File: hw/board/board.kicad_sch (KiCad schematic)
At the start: 21 parts, among them J1 DE9_Receptacle, J2 DE9_Receptacle, J3 DE9_Receptacle, J4 DE9_Receptacle, J5 DE9_Receptacle, J6 DE9_Receptacle, J7 DE9_Receptacle, J8 DE9_Receptacle, U1 XC7A35T-FTG256

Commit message: Added decoupling network following Xiling UG483
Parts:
- added C1, C14, C17, C18, C19, C2, C24, C25, C26, C27, C28, C29, C34, C35, C36, C37, C38, C39, C40: 470n, Capacitor_SMD:C_0805_2012Metric_Pad1.18x1.45mm_HandSolder, symbol Device:C
- added C13, C15: 47u, Capacitor_SMD:C_0805_2012Metric_Pad1.18x1.45mm_HandSolder, symbol Device:C
- added C16: 100u, Capacitor_SMD:C_0805_2012Metric_Pad1.18x1.45mm_HandSolder, symbol Device:C
- added C22, C23, C30, C31, C32, C33: 4u7, Capacitor_SMD:C_0805_2012Metric_Pad1.18x1.45mm_HandSolder, symbol Device:C
- C10, C11, C3: value 4u7 -> 470n; footprint Capacitor_SMD:C_0805_2012Metric -> Capacitor_SMD:C_0805_2012Metric_Pad1.18x1.45mm_HandSolder
- C12: value 100u -> 470n; footprint Capacitor_SMD:C_0805_2012Metric -> Capacitor_SMD:C_0805_2012Metric_Pad1.18x1.45mm_HandSolder
- C20: renamed from C2; footprint Capacitor_SMD:C_0805_2012Metric -> Capacitor_SMD:C_0805_2012Metric_Pad1.18x1.45mm_HandSolder
- C21: renamed from C1; value 100u -> 4u7; footprint Capacitor_SMD:C_0805_2012Metric -> Capacitor_SMD:C_0805_2012Metric_Pad1.18x1.45mm_HandSolder
- C4: value 100u -> 4u7; footprint Capacitor_SMD:C_0805_2012Metric -> Capacitor_SMD:C_0805_2012Metric_Pad1.18x1.45mm_HandSolder
- C5, C7, C8, C9: footprint Capacitor_SMD:C_0805_2012Metric -> Capacitor_SMD:C_0805_2012Metric_Pad1.18x1.45mm_HandSolder
- C6: value 4u7 -> 47u; footprint Capacitor_SMD:C_0805_2012Metric -> Capacitor_SMD:C_0805_2012Metric_Pad1.18x1.45mm_HandSolder
- renumbered J3 to J2, J5 to J3, J7 to J4, J2 to J5, J4 to J6, J6 to J7
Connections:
- net +1V0: now also C10.1, C11.1, C12.1, C7.1, C8.1, C9.1, U1.F7 (VCCINT), U1.F9 (VCCINT), U1.G6 (VCCINT), U1.H9 (VCCINT), U1.J6 (VCCINT), U1.K9 (VCCINT), U1.L8 (VCCINT), C13.1, C14.1
- net +3V3: now also C15.1, C16.1, C17.1, C18.1, C19.1, C22.1, C23.1, C24.1, C25.1, C26.1, C27.1, C28.1, C29.1, C30.1, C31.1, C32.1, C33.1, C34.1, C35.1, C36.1, C37.1, C38.1, C39.1, C40.1; no longer C10.1, C11.1, C12.1, C3.1, C4.1, C5.1, C6.1, C7.1, C8.1, C9.1
- net GND: now also U1.A1 (GND), U1.A11 (GND), U1.B8 (GND), U1.C15 (GND), U1.C5 (GND), U1.D12 (GND), U1.D2 (GND), U1.E9 (GND), U1.F10 (GND), U1.F16 (GND), U1.F6 (GND), U1.F8 (VCCBATT_0), U1.G13 (GND), U1.G3 (GND), U1.G7 (GNDADC_0), U1.G8 (VCCADC_0), U1.G9 (GND), U1.H6 (GND), U1.J11 (GND), U1.J9 (GND), U1.K14 (GND), U1.K4 (GND), U1.K6 (GND), U1.L1 (GND), U1.L11 (GND), U1.M8 (GND), U1.N15 (GND), U1.N5 (GND), U1.P12 (GND), U1.P2 (GND), U1.R9 (GND), U1.T16 (GND), U1.T6 (GND), C1.2, C13.2, C14.2, C15.2, C16.2, C17.2, C18.2, C19.2, C2.2, C22.2, C23.2, C24.2, C25.2, C26.2, C27.2, C28.2, C29.2, C30.2, C31.2, C32.2, C33.2, C34.2, C35.2, C36.2, C37.2, C38.2, C39.2, C40.2
- net +1V8: now reaches U1.G10 (VCCAUX)
- net +1V8: now also C3.1, C4.1, C5.1, C6.1, U1.J10 (VCCAUX), U1.K11 (VCCAUX), U1.L10 (VCCAUX), C1.1, C2.1
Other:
- moved on the sheet: C20, C21, U1A, U1B, U1C, U1D

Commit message: Added DE9 connector footprint
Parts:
- removed C1, C10, C11, C12, C14, C17, C18, C19, C2, C24, C25, C26, C27, C28, C29, C3, C34, C35, C36, C37, C38, C39, C40: 470n, Capacitor_SMD:C_0805_2012Metric_Pad1.18x1.45mm_HandSolder, symbol Device:C
- removed C13, C6: 47u, Capacitor_SMD:C_0805_2012Metric_Pad1.18x1.45mm_HandSolder, symbol Device:C
- removed C16, C7: 100u, Capacitor_SMD:C_0805_2012Metric_Pad1.18x1.45mm_HandSolder, symbol Device:C
- removed C20, C21, C22, C23, C30, C31, C32, C33, C4, C5, C8, C9: 4u7, Capacitor_SMD:C_0805_2012Metric_Pad1.18x1.45mm_HandSolder, symbol Device:C
- removed J1, J2, J3, J4, J5, J6, J7, J8: DE9_Receptacle, DE9:DE9_Pins, symbol Connector:DE9_Receptacle
- removed unit 4 of U1
- renumbered C15 to C1
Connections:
- net +3V3 renamed +2V5
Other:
- added sheet PDN (PDN.kicad_sch)
- added sheet SpW Connection (SpW.kicad_sch)
- moved on the sheet: C1, U1A, U1B, U1C

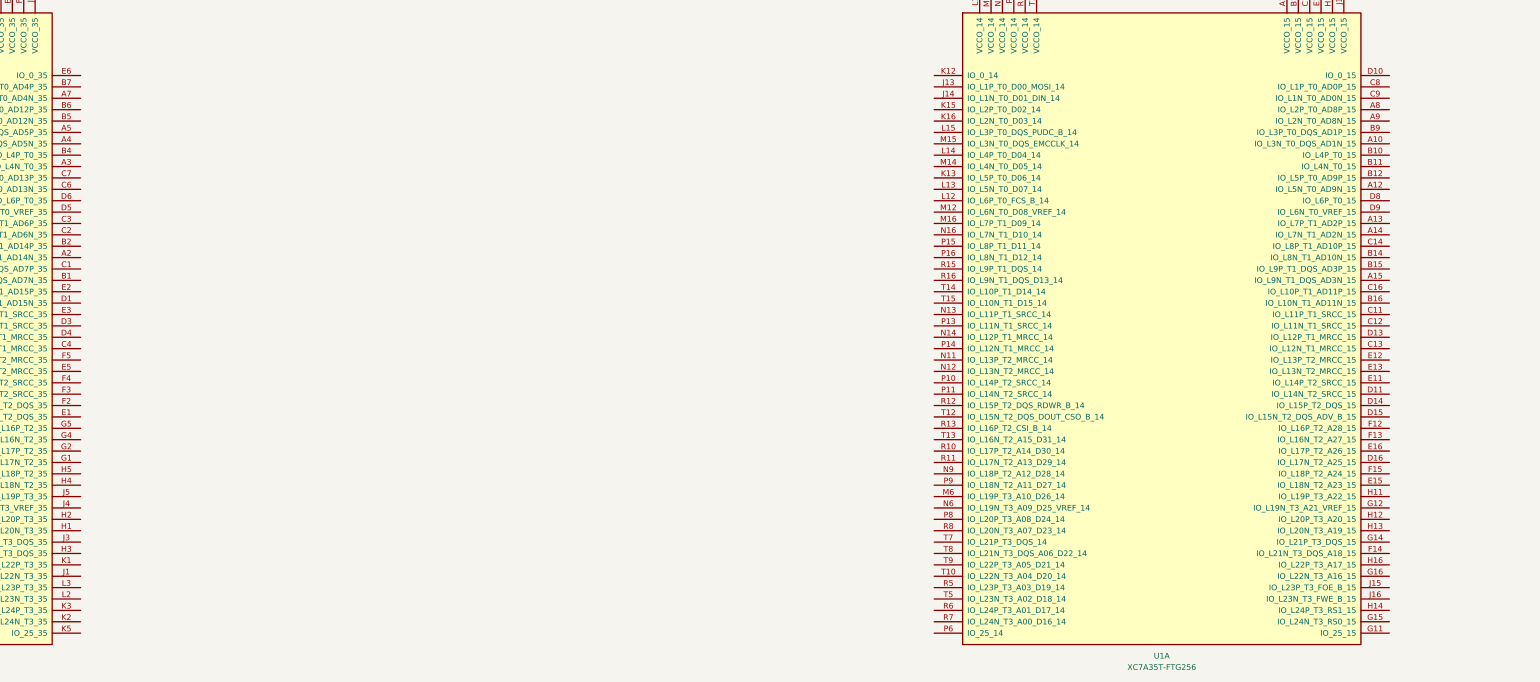
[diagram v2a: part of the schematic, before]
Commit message: Routed DE-9 connectors
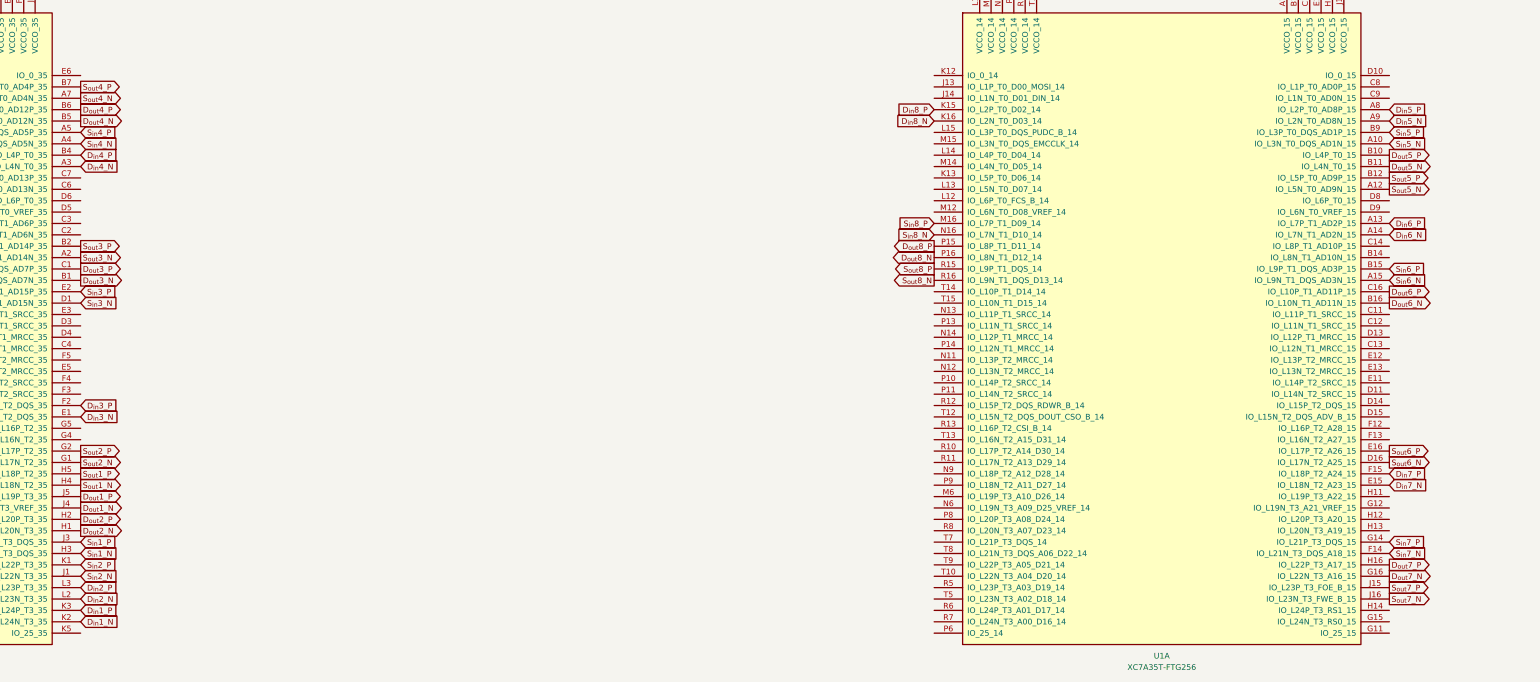
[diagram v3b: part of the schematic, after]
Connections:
- net S_{out}3_N: now reaches U1.A2 (IO_L8N_T1_AD14N_35)
- net D_{in}4_N: now reaches U1.A3 (IO_L4N_T0_35)
- net S_{in}4_N: now reaches U1.A4 (IO_L3N_T0_DQS_AD5N_35)
- net S_{in}4_P: now reaches U1.A5 (IO_L3P_T0_DQS_AD5P_35)
- net S_{out}4_N: now reaches U1.A7 (IO_L1N_T0_AD4N_35)
- net D_{out}3_N: now reaches U1.B1 (IO_L9N_T1_DQS_AD7N_35)
- net S_{out}3_P: now reaches U1.B2 (IO_L8P_T1_AD14P_35)
- net D_{in}4_P: now reaches U1.B4 (IO_L4P_T0_35)
- net D_{out}4_N: now reaches U1.B5 (IO_L2N_T0_AD12N_35)
- net D_{out}4_P: now reaches U1.B6 (IO_L2P_T0_AD12P_35)
- net S_{out}4_P: now reaches U1.B7 (IO_L1P_T0_AD4P_35)
- net D_{out}3_P: now reaches U1.C1 (IO_L9P_T1_DQS_AD7P_35)
- net S_{in}3_N: now reaches U1.D1 (IO_L10N_T1_AD15N_35)
- net D_{in}3_N: now reaches U1.E1 (IO_L15N_T2_DQS_35)
- net S_{in}3_P: now reaches U1.E2 (IO_L10P_T1_AD15P_35)
- net D_{in}3_P: now reaches U1.F2 (IO_L15P_T2_DQS_35)
- net S_{out}2_N: now reaches U1.G1 (IO_L17N_T2_35)
- net S_{out}2_P: now reaches U1.G2 (IO_L17P_T2_35)
- net D_{out}2_N: now reaches U1.H1 (IO_L20N_T3_35)
- net D_{out}2_P: now reaches U1.H2 (IO_L20P_T3_35)
- net S_{in}1_N: now reaches U1.H3 (IO_L21N_T3_DQS_35)
- net S_{out}1_N: now reaches U1.H4 (IO_L18N_T2_35)
- net S_{out}1_P: now reaches U1.H5 (IO_L18P_T2_35)
- net S_{in}2_N: now reaches U1.J1 (IO_L22N_T3_35)
- net S_{in}1_P: now reaches U1.J3 (IO_L21P_T3_DQS_35)
- net D_{out}1_N: now reaches U1.J4 (IO_L19N_T3_VREF_35)
- net D_{out}1_P: now reaches U1.J5 (IO_L19P_T3_35)
- net S_{in}2_P: now reaches U1.K1 (IO_L22P_T3_35)
- net D_{in}1_N: now reaches U1.K2 (IO_L24N_T3_35)
- net D_{in}1_P: now reaches U1.K3 (IO_L24P_T3_35)
- net D_{in}2_N: now reaches U1.L2 (IO_L23N_T3_35)
- net D_{in}2_P: now reaches U1.L3 (IO_L23P_T3_35)
- net S_{in}5_N: now reaches U1.A10 (IO_L3N_T0_DQS_AD1N_15)
- net S_{out}5_N: now reaches U1.A12 (IO_L5N_T0_AD9N_15)
- net D_{in}6_P: now reaches U1.A13 (IO_L7P_T1_AD2P_15)
- net D_{in}6_N: now reaches U1.A14 (IO_L7N_T1_AD2N_15)
- net S_{in}6_N: now reaches U1.A15 (IO_L9N_T1_DQS_AD3N_15)
- net D_{in}5_P: now reaches U1.A8 (IO_L2P_T0_AD8P_15)
- net D_{in}5_N: now reaches U1.A9 (IO_L2N_T0_AD8N_15)
- net D_{out}5_P: now reaches U1.B10 (IO_L4P_T0_15)
- net D_{out}5_N: now reaches U1.B11 (IO_L4N_T0_15)
- net S_{out}5_P: now reaches U1.B12 (IO_L5P_T0_AD9P_15)
- net S_{in}6_P: now reaches U1.B15 (IO_L9P_T1_DQS_AD3P_15)
- net D_{out}6_N: now reaches U1.B16 (IO_L10N_T1_AD11N_15)
- net S_{in}5_P: now reaches U1.B9 (IO_L3P_T0_DQS_AD1P_15)
- net D_{out}6_P: now reaches U1.C16 (IO_L10P_T1_AD11P_15)
- net S_{out}6_N: now reaches U1.D16 (IO_L17N_T2_A25_15)
- net D_{in}7_N: now reaches U1.E15 (IO_L18N_T2_A23_15)
- net S_{out}6_P: now reaches U1.E16 (IO_L17P_T2_A26_15)
- net S_{in}7_N: now reaches U1.F14 (IO_L21N_T3_DQS_A18_15)
- net D_{in}7_P: now reaches U1.F15 (IO_L18P_T2_A24_15)
- net S_{in}7_P: now reaches U1.G14 (IO_L21P_T3_DQS_15)
- net D_{out}7_N: now reaches U1.G16 (IO_L22N_T3_A16_15)
- net D_{out}7_P: now reaches U1.H16 (IO_L22P_T3_A17_15)
- net S_{out}7_P: now reaches U1.J15 (IO_L23P_T3_FOE_B_15)
- net S_{out}7_N: now reaches U1.J16 (IO_L23N_T3_FWE_B_15)
- net D_{in}8_P: now reaches U1.K15 (IO_L2P_T0_D02_14)
- net D_{in}8_N: now reaches U1.K16 (IO_L2N_T0_D03_14)
- net S_{in}8_P: now reaches U1.M16 (IO_L7P_T1_D09_14)
- net S_{in}8_N: now reaches U1.N16 (IO_L7N_T1_D10_14)
- net D_{out}8_P: now reaches U1.P15 (IO_L8P_T1_D11_14)
- net D_{out}8_N: now reaches U1.P16 (IO_L8N_T1_D12_14)
- net S_{out}8_P: now reaches U1.R15 (IO_L9P_T1_DQS_14)
- net S_{out}8_N: now reaches U1.R16 (IO_L9N_T1_DQS_D13_14)

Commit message: Began routing decoupling network
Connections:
- net +2V5: no longer U1.A16 (VCCO_15), U1.A6 (VCCO_35), U1.B13 (VCCO_15), U1.B3 (VCCO_35), U1.C10 (VCCO_15), U1.D7 (VCCO_35), U1.E14 (VCCO_15), U1.E4 (VCCO_35), U1.F1 (VCCO_35), U1.H15 (VCCO_15), U1.J12 (VCCO_15), U1.J2 (VCCO_35), U1.L16 (VCCO_14), U1.M13 (VCCO_14), U1.N10 (VCCO_14), U1.P7 (VCCO_14), U1.R14 (VCCO_14), U1.T11 (VCCO_14)
- new net VCCO_14: U1.L16 (VCCO_14), U1.M13 (VCCO_14), U1.N10 (VCCO_14), U1.P7 (VCCO_14), U1.R14 (VCCO_14), U1.T11 (VCCO_14)
- new net VCCO_15: U1.A16 (VCCO_15), U1.B13 (VCCO_15), U1.C10 (VCCO_15), U1.E14 (VCCO_15), U1.H15 (VCCO_15), U1.J12 (VCCO_15)
- new net VCCO_35: U1.A6 (VCCO_35), U1.B3 (VCCO_35), U1.D7 (VCCO_35), U1.E4 (VCCO_35), U1.F1 (VCCO_35), U1.J2 (VCCO_35)
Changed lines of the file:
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@@
 		)
 	)
+	(global_label "VCCO_14"
+		(shape input)
+		(at 344.17 137.16 90)
+		(fields_autoplaced yes)
+		(effects
+			(font
+				(size 1.27 1.27)
+			)
+			(justify left)
+		)
+		(property "Intersheetrefs" "${INTERSHEET_REFS}"
+			(at 344.17 125.8291 90)
+			(effects
+				(font
+					(size 1.27 1.27)
+				)
+				(justify left)
+				(hide yes)
+			)
+		)
+	)
 	(global_label "D_{out}2_P"
 		(shape output)
@@
 		)
 	)
+	(global_label "VCCO_15"
+		(shape input)
+		(at 425.45 137.16 90)
+		(fields_autoplaced yes)
+		(effects
+			(font
+				(size 1.27 1.27)
+			)
+			(justify left)
+		)
+		(property "Intersheetrefs" "${INTERSHEET_REFS}"
+			(at 425.45 125.8291 90)
+			(effects
+				(font
+					(size 1.27 1.27)
+				)
+				(justify left)
+				(hide yes)
+			)
+		)
+	)
 	(global_label "S_{out}5_P"
 		(shape output)
@@
 		)
 	)
+	(global_label "VCCO_35"
+		(shape input)
+		(at 133.35 137.16 90)
+		(fields_autoplaced yes)
+		(effects
+			(font
+				(size 1.27 1.27)
+			)
+			(justify left)
+		)
+		(property "Intersheetrefs" "${INTERSHEET_REFS}"
+			(at 133.35 125.8291 90)
+			(effects
+				(font
+					(size 1.27 1.27)
+				)
+				(justify left)
+				(hide yes)
+			)
+		)
+	)
 	(global_label "S_{out}1_P"
 		(shape output)
@@
 	)
 	(symbol
-		(lib_id "power:+2V5")
-		(at 425.45 137.16 0)
-		(unit 1)
-		(exclude_from_sim no)
-		(in_bom yes)
-		(on_board yes)
-		(dnp no)
-		(fields_autoplaced yes)
-		(property "Reference" "#PWR014"
-			(at 425.45 140.97 0)
-			(effects
-				(font
-					(size 1.27 1.27)
-				)
-				(hide yes)
-			)
-		)
-		(property "Value" "+2V5"
-			(at 425.45 132.08 0)
-			(effects
-				(font
-					(size 1.27 1.27)
-				)
-			)
-		)
-		(property "Footprint" ""
-			(at 425.45 137.16 0)
-			(effects
-				(font
-					(size 1.27 1.27)
-				)
-				(hide yes)
-			)
-		)
-		(property "Datasheet" ""
-			(at 425.45 137.16 0)
-			(effects
-				(font
-					(size 1.27 1.27)
-				)
-				(hide yes)
-			)
-		)
-		(property "Description" "Power symbol creates a global label with name \"+2V5\""
-			(at 425.45 137.16 0)
-			(effects
-				(font
-					(size 1.27 1.27)
-				)
-				(hide yes)
-			)
-		)
-		(pin "1"
-		)
-		(instances
-			(project "board"
-				(path "/0e384709-6bce-4dbf-a0e0-550e970390f4"
-					(reference "#PWR014")
-					(unit 1)
-				)
-			)
-		)
-	)
-	(symbol
 		(lib_id "FPGA_Xilinx_Artix7:XC7A35T-FTG256")
 		(at 92.71 220.98 0)
@@
 	)
 	(symbol
-		(lib_id "power:+2V5")
-		(at 133.35 137.16 0)
-		(unit 1)
-		(exclude_from_sim no)
-		(in_bom yes)
-		(on_board yes)
-		(dnp no)
-		(fields_autoplaced yes)
-		(property "Reference" "#PWR09"
-			(at 133.35 140.97 0)
-			(effects
-				(font
-					(size 1.27 1.27)
-				)
-				(hide yes)
-			)
-		)
-		(property "Value" "+2V5"
-			(at 133.35 132.08 0)
-			(effects
-				(font
-					(size 1.27 1.27)
-				)
-			)
-		)
-		(property "Footprint" ""
-			(at 133.35 137.16 0)
-			(effects
-				(font
-					(size 1.27 1.27)
-				)
-				(hide yes)
-			)
-		)
-		(property "Datasheet" ""
-			(at 133.35 137.16 0)
-			(effects
-				(font
-					(size 1.27 1.27)
-				)
-				(hide yes)
-			)
-		)
-		(property "Description" "Power symbol creates a global label with name \"+2V5\""
-			(at 133.35 137.16 0)
-			(effects
-				(font
-					(size 1.27 1.27)
-				)
-				(hide yes)
-			)
-		)
-		(pin "1"
-		)
-		(instances
-			(project "board"
-				(path "/0e384709-6bce-4dbf-a0e0-550e970390f4"
-					(reference "#PWR09")
-					(unit 1)
-				)
-			)
-		)
-	)
-	(symbol
 		(lib_id "FPGA_Xilinx_Artix7:XC7A35T-FTG256")
 		(at 501.65 72.39 0)
@@
 					(unit 1)
 				)
-			)
-		)
-	)
-	(symbol
-		(lib_id "power:+2V5")
-		(at 344.17 137.16 0)
-		(unit 1)
-		(exclude_from_sim no)
-		(in_bom yes)
-		(on_board yes)
-		(dnp no)
-		(fields_autoplaced yes)
-		(property "Reference" "#PWR013"
-			(at 344.17 140.97 0)
-			(effects
-				(font
-					(size 1.27 1.27)
-				)
-				(hide yes)
-			)
-		)
-		(property "Value" "+2V5"
-			(at 344.17 132.08 0)
-			(effects
-				(font
-					(size 1.27 1.27)
-				)
-			)
-		)
-		(property "Footprint" ""
-			(at 344.17 137.16 0)
-			(effects
-				(font
-					(size 1.27 1.27)
-				)
-				(hide yes)
-			)
-		)
-		(property "Datasheet" ""
-			(at 344.17 137.16 0)
-			(effects
-				(font
-					(size 1.27 1.27)
-				)
-				(hide yes)
-			)
-		)
-		(property "Description" "Power symbol creates a global label with name \"+2V5\""
-			(at 344.17 137.16 0)
-			(effects
-				(font
-					(size 1.27 1.27)
-				)
-				(hide yes)
-			)
-		)
-		(pin "1"
-		)
-		(instances
-			(project "board"
-				(path "/0e384709-6bce-4dbf-a0e0-550e970390f4"
-					(reference "#PWR013")
-					(unit 1)
-				)

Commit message: Routed decoupling capacitors
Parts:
- C1: footprint Capacitor_SMD:C_0805_2012Metric_Pad1.18x1.45mm_HandSolder -> Capacitor_SMD:C_0805_2012Metric
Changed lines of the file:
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@@
 			)
 		)
-		(property "Footprint" "Capacitor_SMD:C_0805_2012Metric_Pad1.18x1.45mm_HandSolder"
+		(property "Footprint" "Capacitor_SMD:C_0805_2012Metric"
 			(at 539.4452 39.37 0)
 			(effects

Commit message: Finished routing STM32 connection, resolved DRC errors
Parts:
- added C15: 47u, Capacitor_SMD:C_0805_2012Metric, symbol Device:C
- added C17: 470n, Capacitor_SMD:C_0805_2012Metric, symbol Device:C
- added U5: STM32F302CBTx, Package_QFP:LQFP-48_7x7mm_P0.5mm, symbol MCU_ST_STM32F3:STM32F302CBTx
- added U6: W25Q128JVSIQTR, EasyEDA:SOIC-8_L5.3-W5.3-P1.27-LS8.0-BL, symbol EasyEDA:W25Q128JVSIQTR
- added USB1: TYPE-C 16PIN 2MD(073), EasyEDA:USB-C-SMD_TYPE-C-6PIN-2MD-073, symbol EasyEDA:TYPE-C16PIN2MD(073)
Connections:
- net +2V5: now also U1.M10 (M1_0), U1.M11 (M2_0), U1.M9 (M0_0), C15.1, C17.1, U6.8 (VCC)
- net D_{out}1_N: now also U1.D3 (IO_L11N_T1_SRCC_35); no longer U1.J4 (IO_L19N_T3_VREF_35)
- net D_{out}1_P: now also U1.E3 (IO_L11P_T1_SRCC_35); no longer U1.J5 (IO_L19P_T3_35)
- net GND: now also C15.2, C17.2, U6.4 (GND), USB1.1 (GND), USB1.12 (GND), USB1.13 (SHELL), USB1.14 (SHELL)
- net S_{out}1_N: now also U1.C2 (IO_L7N_T1_AD6N_35); no longer U1.H4 (IO_L18N_T2_35)
- net S_{out}1_P: now also U1.C3 (IO_L7P_T1_AD6P_35); no longer U1.H5 (IO_L18P_T2_35)
- net DIN: now reaches U1.J14 (IO_L1N_T0_D01_DIN_14)
- net DIN: now also U5.17 (PA7)
- net CCLK: now reaches U1.E8 (CCLK_0)
- net CCLK: now also U5.15 (PA5)
- net DONE: now reaches U1.H10 (DONE_0)
- net DONE: now also U5.10 (PA0)
- net INIT_B: now reaches U1.K10 (INIT_B_0)
- net INIT_B: now also U5.12 (PA2)
- net TCK: now reaches U1.L7 (TCK_0)
- net PROGRAM_B: now reaches U1.L9 (PROGRAM_B_0)
- net PROGRAM_B: now also U5.11 (PA1)
- net TMS: now reaches U1.M7 (TMS_0)
- net TDI: now reaches U1.N7 (TDI_0)
- net TDO: now reaches U1.N8 (TDO_0)
- new net: U5.23 (VSS), U5.35 (VSS), U5.47 (VSS)
- new net FLASH_MISO: U5.27 (PB14), U6.2 (DO)
- new net FLASH_MOSI: U5.28 (PB15), U6.5 (DI)
- new net FLASH_SCK: U5.26 (PB13), U6.6 (CLK)
- new net USB_D_N: U5.32 (PA11), USB1.7 (DN1)
- new net USB_D_P: U5.33 (PA12), USB1.6 (DP1)
- new net ~{FLASH_CS}: U5.25 (PB12), U6.1 (~{CS})
- no-connect marks 0 -> 10
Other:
- added sheet STM32 (stm32.kicad_sch)
- moved on the sheet: C1, U1C
